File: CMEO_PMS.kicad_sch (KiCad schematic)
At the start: 0 parts

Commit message: CMEO_PMS Board V1.0 REV A
Completed first iteration of CMEO PMS board
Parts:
- added C1, C10, C2, C3, C4, C5, C6, C7, C8, C9: 10nF, Capacitor_SMD:C_0805_2012Metric, symbol Device:C_Polarized
- added D1: D, CMEO_PMS:DFLR1400-7, symbol Device:D
- added H1, H2, H3, H4: MH, MountingHole:MountingHole_3.2mm_M3, symbol Mechanical:MountingHole
- added J1, J2: Conn_01x02, Connector_PinHeader_2.54mm:PinHeader_1x02_P2.54mm_Vertical, symbol Connector_Generic:Conn_01x02
- added T1: B78310P8078A002, CMEO_PMS:B78310P8078A002, symbol B78310P8078A002_Transformer:B78310P8078A002_Trans
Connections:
- new net: C6.2, C7.1
- new net: C7.2, C8.1
- new net: C4.2, C5.1
- new net: C5.2, C6.1
- new net: C2.2, C3.1
- new net: C3.2, C4.1
- new net: C8.2, C9.1
- new net: C10.1, C9.2
- new net: C1.2, C2.1
- new net GND1: J1.1 (Pin_1), T1.1 (W2')
- new net GND2: C10.2, J2.2 (Pin_2), T1.6 (W1)
- new net MS_RTENG_OUT: J1.2 (Pin_2), T1.3 (W2)
- new net V_OUT: C1.1, D1.1 (K), J2.1 (Pin_1)
- new net W1': D1.2 (A), T1.4 (W1')
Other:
- note added: "10 Series Caps: 1/10 eq. C = 1nF Estimated per Cap load: 25V -> C loss: <5% =~ 0.8nF MS-RTENG Eq. C ~ 10pF After 1:8 Trans: C ~ 0.64nF"
- note added: "CL21B103KBANNNC Capacitors Rated 50V"
- note added: "Connect to MS-RTENG"
- note added: "DFLR1400-7"
- note added: "MS-RTENG Eq. Impedance = 10pF"
- note added: "Mounting Holes"

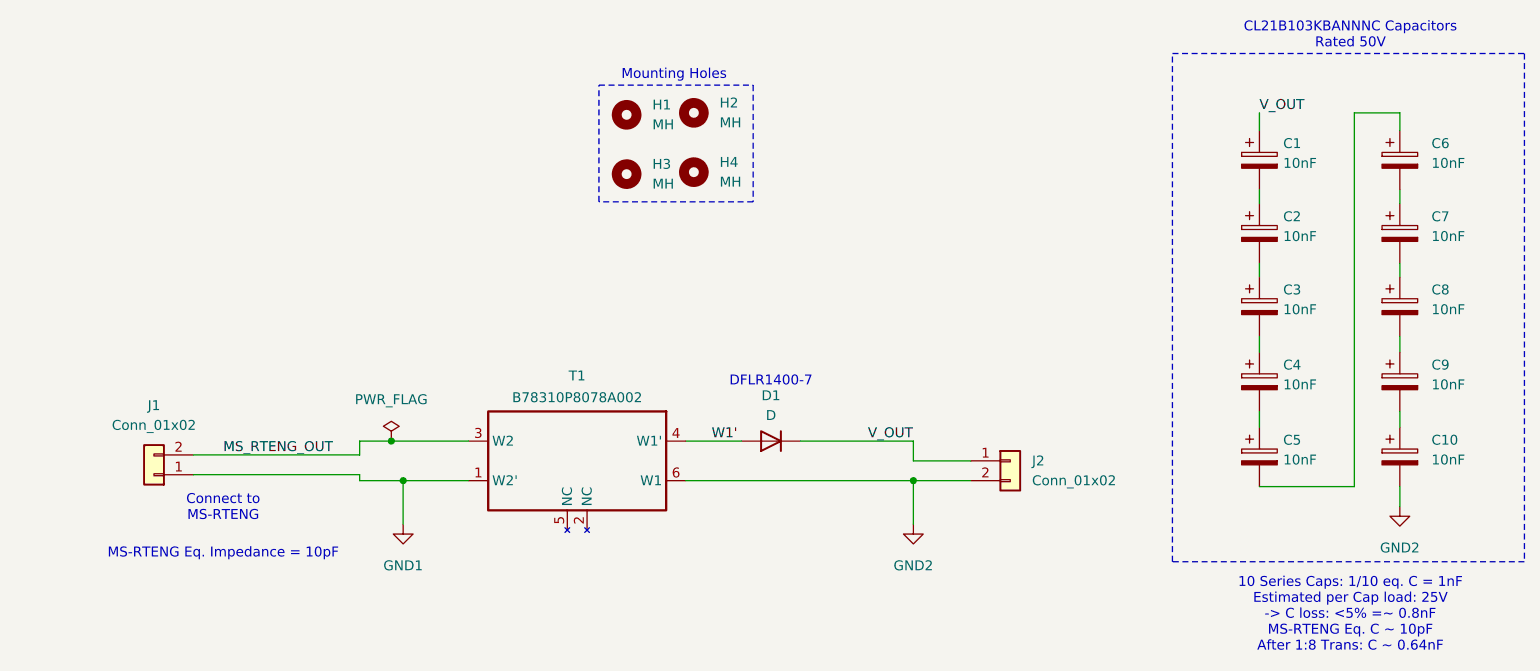
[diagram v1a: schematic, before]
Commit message: CMEO_PMS Board V1.0 REV B
- Separated input and output headers to reduce risk of high voltage breakdown
- Increased fill gap to 2mm to reduce risk of high voltage breakdown
- Changed diode to THT for easier soldering
- Changed capacitor to 10uF, 400V limit. increase in capacitance is to better act as a battery for power purposes
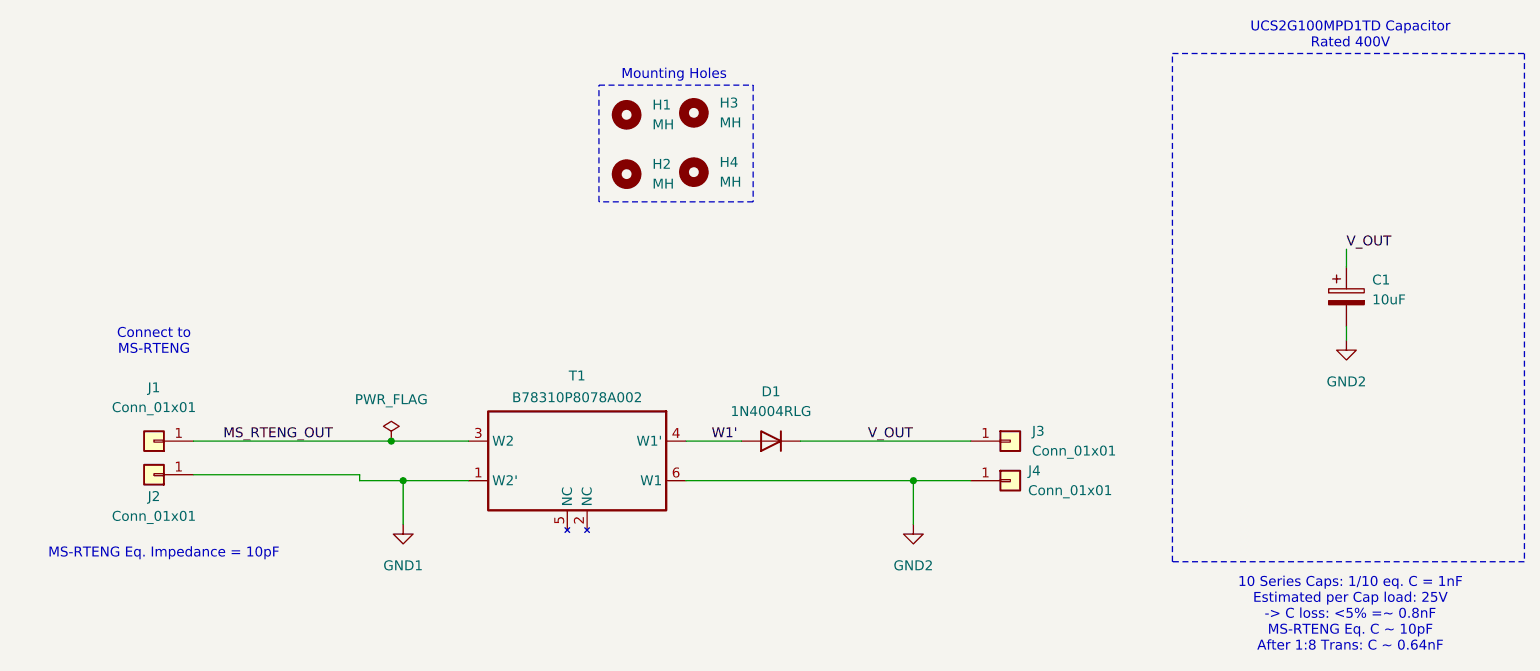
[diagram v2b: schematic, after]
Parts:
- removed C10, C2, C3, C4, C5, C6, C7, C8, C9: 10nF, Capacitor_SMD:C_0805_2012Metric, symbol Device:C_Polarized
- removed J1, J2: Conn_01x02, Connector_PinHeader_2.54mm:PinHeader_1x02_P2.54mm_Vertical, symbol Connector_Generic:Conn_01x02
- added J1, J2, J3, J4: Conn_01x01, Connector_PinHeader_2.54mm:PinHeader_1x01_P2.54mm_Vertical, symbol Connector_Generic:Conn_01x01
- C1: value 10nF -> 10uF; footprint Capacitor_SMD:C_0805_2012Metric -> Capacitor_THT:CP_Radial_D10.0mm_P5.00mm
- D1: value D -> 1N4004RLG; footprint CMEO_PMS:DFLR1400-7 -> Diode_THT:D_DO-41_SOD81_P7.62mm_Horizontal
- renumbered H3 to H2, H2 to H3
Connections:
- net GND1: now also J2.1 (Pin_1)
- net GND2: now also C1.2, J4.1 (Pin_1)
- net MS_RTENG_OUT: now also J1.1 (Pin_1)
- net V_OUT: now also J3.1 (Pin_1)
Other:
- note added: "UCS2G100MPD1TD Capacitor Rated 400V"
- note removed: "CL21B103KBANNNC Capacitors Rated 50V"
- note removed: "DFLR1400-7"
- moved on the sheet: C1
